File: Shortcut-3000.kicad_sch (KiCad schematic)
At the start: 47 parts, among them J1 MagneticPogo_1x05_Female, J10 MagneticPogo_1x05_Female, J11 MagneticPogo_1x05_Female, J12 MagneticPogo_1x05_Female, J2 MagneticPogo_1x05_Female, J3 MagneticPogo_1x05_Female, J4 MagneticPogo_1x05_Female, J5 MagneticPogo_1x05_Female, J6 MagneticPogo_1x05_Female, J7 MagneticPogo_1x05_Female, J8 MagneticPogo_1x05_Female, J9 MagneticPogo_1x05_Female, SW1 SW_Push, SW10 SW_Push, SW11 SW_Push, SW12 SW_Push, SW13 SW_Push, SW14 SW_Push, SW15 SW_Push, SW16 RotaryEncoder_Switch, SW17 RotaryEncoder_Switch, SW2 SW_Push, SW3 SW_Push, SW4 SW_Push, SW5 SW_Push, SW6 SW_Push, SW7 SW_Push, SW8 SW_Push, SW9 SW_Push

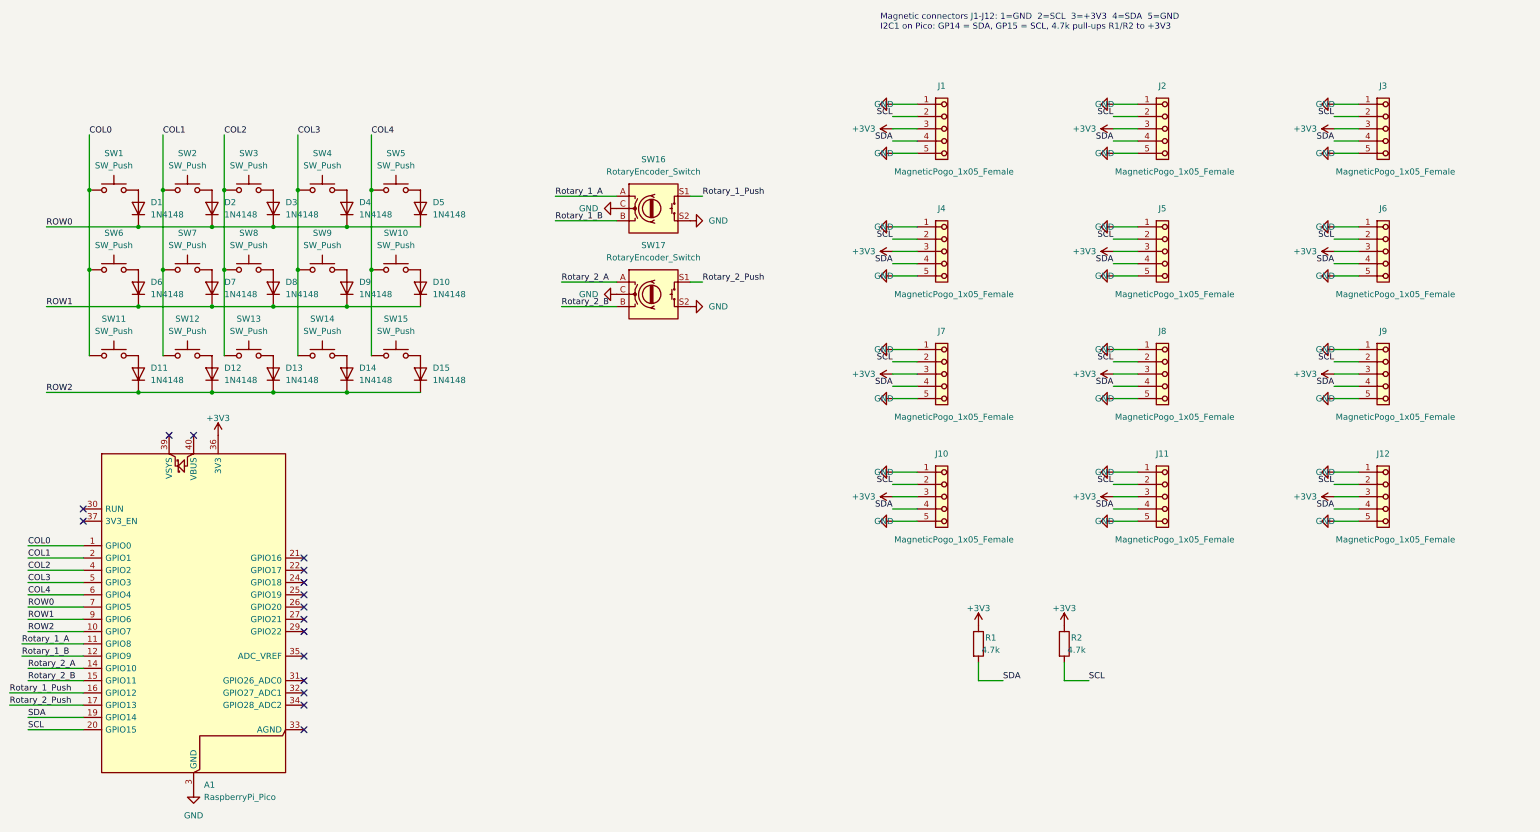
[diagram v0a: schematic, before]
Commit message: Lay out magnetic connectors as a 4x3 module grid
Schematic: J1-J12 rearranged into 4 columns x 3 rows (J1-J4 top row).
PCB: J1-J12 placed on a 25.4mm-pitch grid, each connector centred
along the top edge of its cell with N (pin 1) on the left. Cell
outlines drawn on Cmts.User. Pico GP14/GP15/3V3 pads now carry the
SDA/SCL/+3V3 nets.
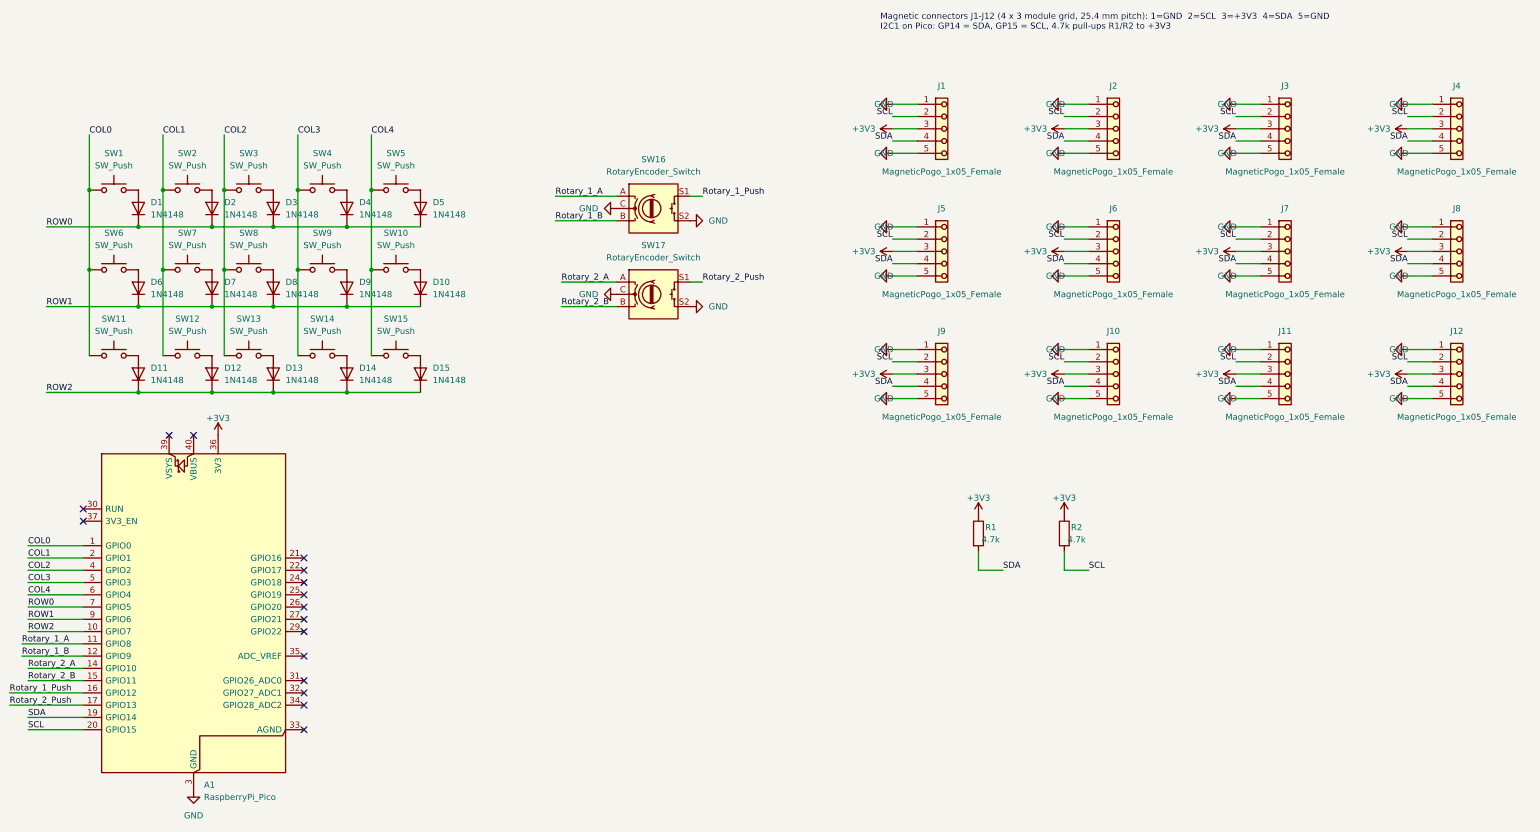
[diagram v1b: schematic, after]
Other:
- note added: "Magnetic connectors J1-J12 (4 x 3 module grid, 25.4 mm pitch): 1=GND 2=SCL 3=+3V3 4=SDA 5=GND I2C1 on Pico: GP14 = SDA, GP15 = SCL, 4.7k pull-ups R1/R2 to +3V3"
- note removed: "Magnetic connectors J1-J12: 1=GND 2=SCL 3=+3V3 4=SDA 5=GND I2C1 on Pico: GP14 = SDA, GP15 = SCL, 4.7k pull-ups R1/R2 to +3V3"
